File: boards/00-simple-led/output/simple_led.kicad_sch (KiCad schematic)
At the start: 3 parts, among them J1 PWR

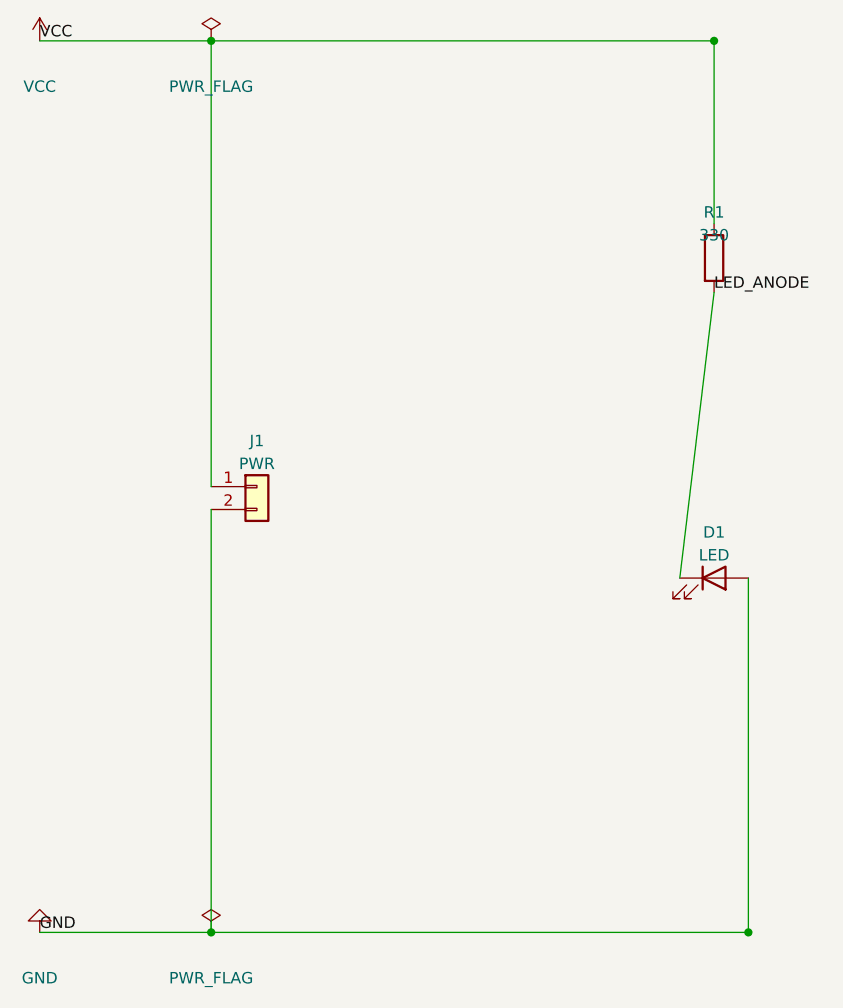
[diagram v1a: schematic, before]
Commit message: fix(board-00): swap D1 wire endpoints so schematic polarity matches PCB
The schematic generator wired R1.2 to D1 pin 1 (K, cathode) and D1 pin 2
(A, anode) to GND, leaving the LED reverse-biased per the schematic. The
PCB generator at generate_led("D1", D1_POS, "LED_ANODE", "GND") already
binds pad 1 to GND and pad 2 to LED_ANODE (forward biased), so the two
halves of the recipe disagreed.

Swap the two D1 wire endpoints in create_led_schematic() and source x_d1
from d1_pin1[0] so the GND-rail junction stays on D1's cathode column.
Also add a fast regression test (TestBoard00D1Polarity) that asserts:

  - Schematic: D1.1 is on net 'GND'; D1.2 is on net 'LED_ANODE'
  - PCB: pad 1 is on net 3 'GND'; pad 2 is on net 2 'LED_ANODE'

Regenerated board 00 output/ artifacts so the demo site and committed
goldens reflect the fix. ERC + DRC still pass; LED_ANODE deterministic
rewrite (_rewrite_led_anode_route) is unaffected because it does PCB
pad-net lookups by net_name, not pin number.

Closes #3747

Co-Authored-By: Claude Opus 4.7 <noreply@anthropic.com>
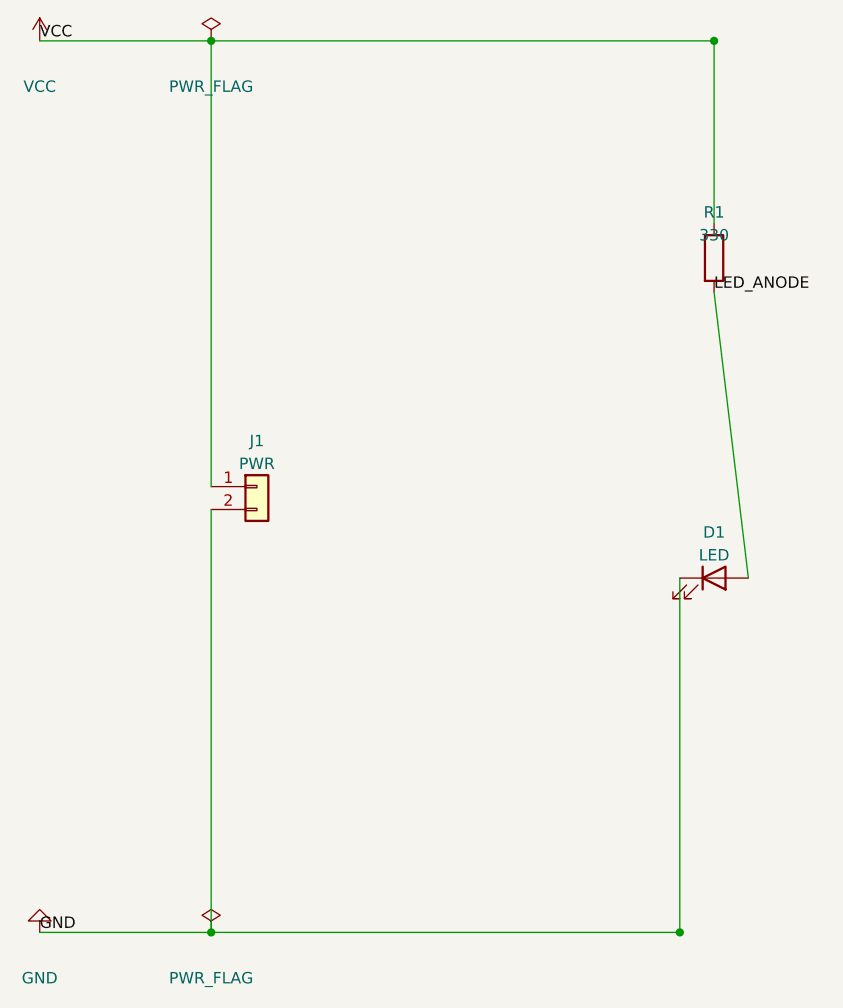
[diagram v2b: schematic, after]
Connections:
- net GND: now also D1.1 (K); no longer D1.2 (A)
- net LED_ANODE: now also D1.2 (A); no longer D1.1 (K)
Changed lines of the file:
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@@
 		(instances
 			(project "project"
-				(path "/14173038-f4e1-435c-a17b-4d5e5cbb9c2f" (reference "J1") (unit 1)
+				(path "/288fa888-be50-4875-a3b3-910af6ab28bb" (reference "J1") (unit 1)
 				)
 			)
@@
 		(instances
 			(project "project"
-				(path "/14173038-f4e1-435c-a17b-4d5e5cbb9c2f" (reference "R1") (unit 1)
+				(path "/288fa888-be50-4875-a3b3-910af6ab28bb" (reference "R1") (unit 1)
 				)
 			)
@@
 		(instances
 			(project "project"
-				(path "/14173038-f4e1-435c-a17b-4d5e5cbb9c2f" (reference "D1") (unit 1)
+				(path "/288fa888-be50-4875-a3b3-910af6ab28bb" (reference "D1") (unit 1)
 				)
 			)
@@
 		(instances
 			(project "project"
-				(path "/14173038-f4e1-435c-a17b-4d5e5cbb9c2f" (reference "#PWR01") (unit 1)
+				(path "/288fa888-be50-4875-a3b3-910af6ab28bb" (reference "#PWR01") (unit 1)
 				)
 			)
@@
 		(instances
 			(project "project"
-				(path "/14173038-f4e1-435c-a17b-4d5e5cbb9c2f" (reference "#PWR02") (unit 1)
+				(path "/288fa888-be50-4875-a3b3-910af6ab28bb" (reference "#PWR02") (unit 1)
 				)
 			)
@@
 		(instances
 			(project "project"
-				(path "/14173038-f4e1-435c-a17b-4d5e5cbb9c2f" (reference "#PWR03") (unit 1)
+				(path "/288fa888-be50-4875-a3b3-910af6ab28bb" (reference "#PWR03") (unit 1)
 				)
 			)
@@
 		(instances
 			(project "project"
-				(path "/14173038-f4e1-435c-a17b-4d5e5cbb9c2f" (reference "#PWR04") (unit 1)
+				(path "/288fa888-be50-4875-a3b3-910af6ab28bb" (reference "#PWR04") (unit 1)
 				)
 			)
@@
 	)
 	(wire
-		(pts (xy 44.45 129.54) (xy 104.14 129.54))
+		(pts (xy 44.45 129.54) (xy 96.52 129.54))
 		(stroke
 			(width 0)
@@
 	)
 	(wire
-		(pts (xy 100.33 58.42) (xy 96.52 90.17))
-		(stroke
-			(width 0)
-			(type default)
-		)
-	)
-	(wire
-		(pts (xy 104.14 90.17) (xy 104.14 129.54))
+		(pts (xy 100.33 58.42) (xy 104.14 90.17))
+		(stroke
+			(width 0)
+			(type default)
+		)
+	)
+	(wire
+		(pts (xy 96.52 90.17) (xy 96.52 129.54))
 		(stroke
 			(width 0)
@@
 	)
 	(junction
-		(at 104.14 129.54)
+		(at 96.52 129.54)
 		(diameter 0)
 	)
@@
 	)
 	(sheet_instances
-		(path "/14173038-f4e1-435c-a17b-4d5e5cbb9c2f" (page "1")
-		)
-	)
+		(path "/288fa888-be50-4875-a3b3-910af6ab28bb" (page "1")
+		)
+	)
